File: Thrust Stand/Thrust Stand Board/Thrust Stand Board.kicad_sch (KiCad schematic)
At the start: 0 parts

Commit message: Components added for Thrust Stand Board
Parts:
- added J1: Conn_01x02_Socket, Package_QFP:TQFP-44_10x10mm_P0.8mm, symbol Connector:Conn_01x02_Socket
- added P1: USB_C_Plug_USB2.0, Package_DFN_QFN:UQFN-16_1.8x2.6mm_P0.4mm, symbol Connector:USB_C_Plug_USB2.0
- added U1: INA238, Package_SO:TSSOP-10_3x3mm_P0.5mm, symbol Sensor_Energy:INA238
- added U2: ACS758xCB-050B-PFF, Sensor_Current:Allegro_CB_PFF, symbol Sensor_Current:ACS758xCB-050B-PFF
- added U3: HX711, Package_SO:SOIC-16_3.9x9.9mm_P1.27mm, symbol Analog_ADC:HX711
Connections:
- new net: P1.A4 (VBUS), P1.A9 (VBUS), P1.B4 (VBUS), P1.B9 (VBUS)
- new net +BATT: J1.2 (Pin_2), U1.8 (Vbus)
- new net GND: J1.1 (Pin_1), P1.A1 (GND), P1.A12 (GND), P1.B1 (GND), P1.B12 (GND), P1.SH (SHIELD), U1.7 (GND)
- new net USBC_N: P1.A7 (D-)
- new net USBC_P: P1.A6 (D+)

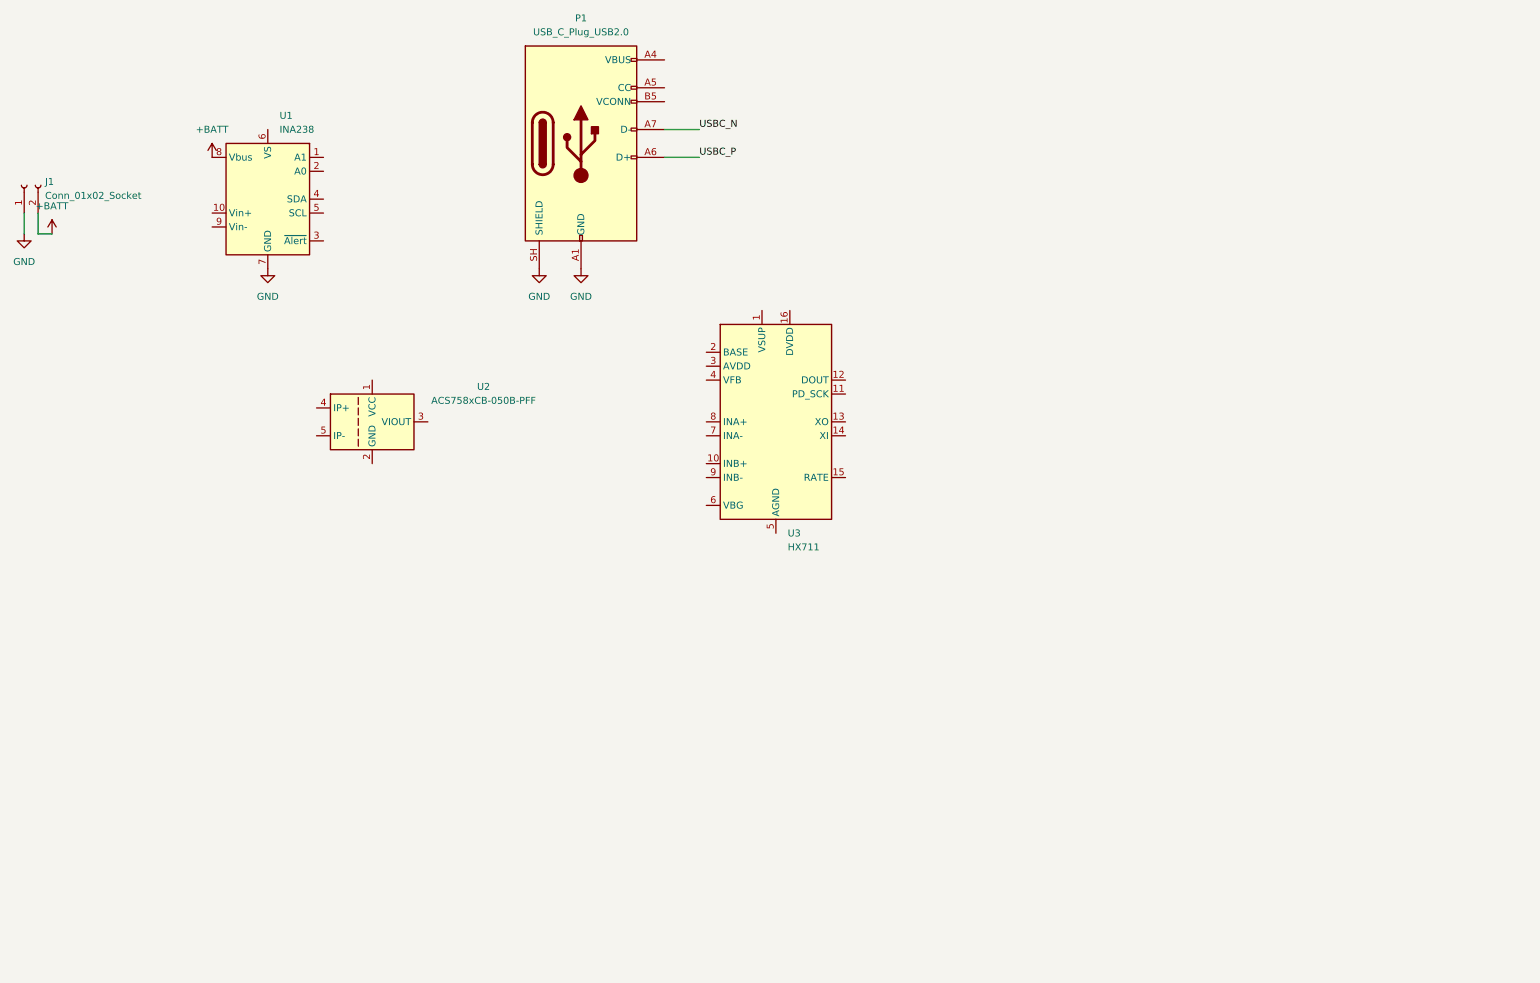
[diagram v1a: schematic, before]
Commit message: Schematic Updates
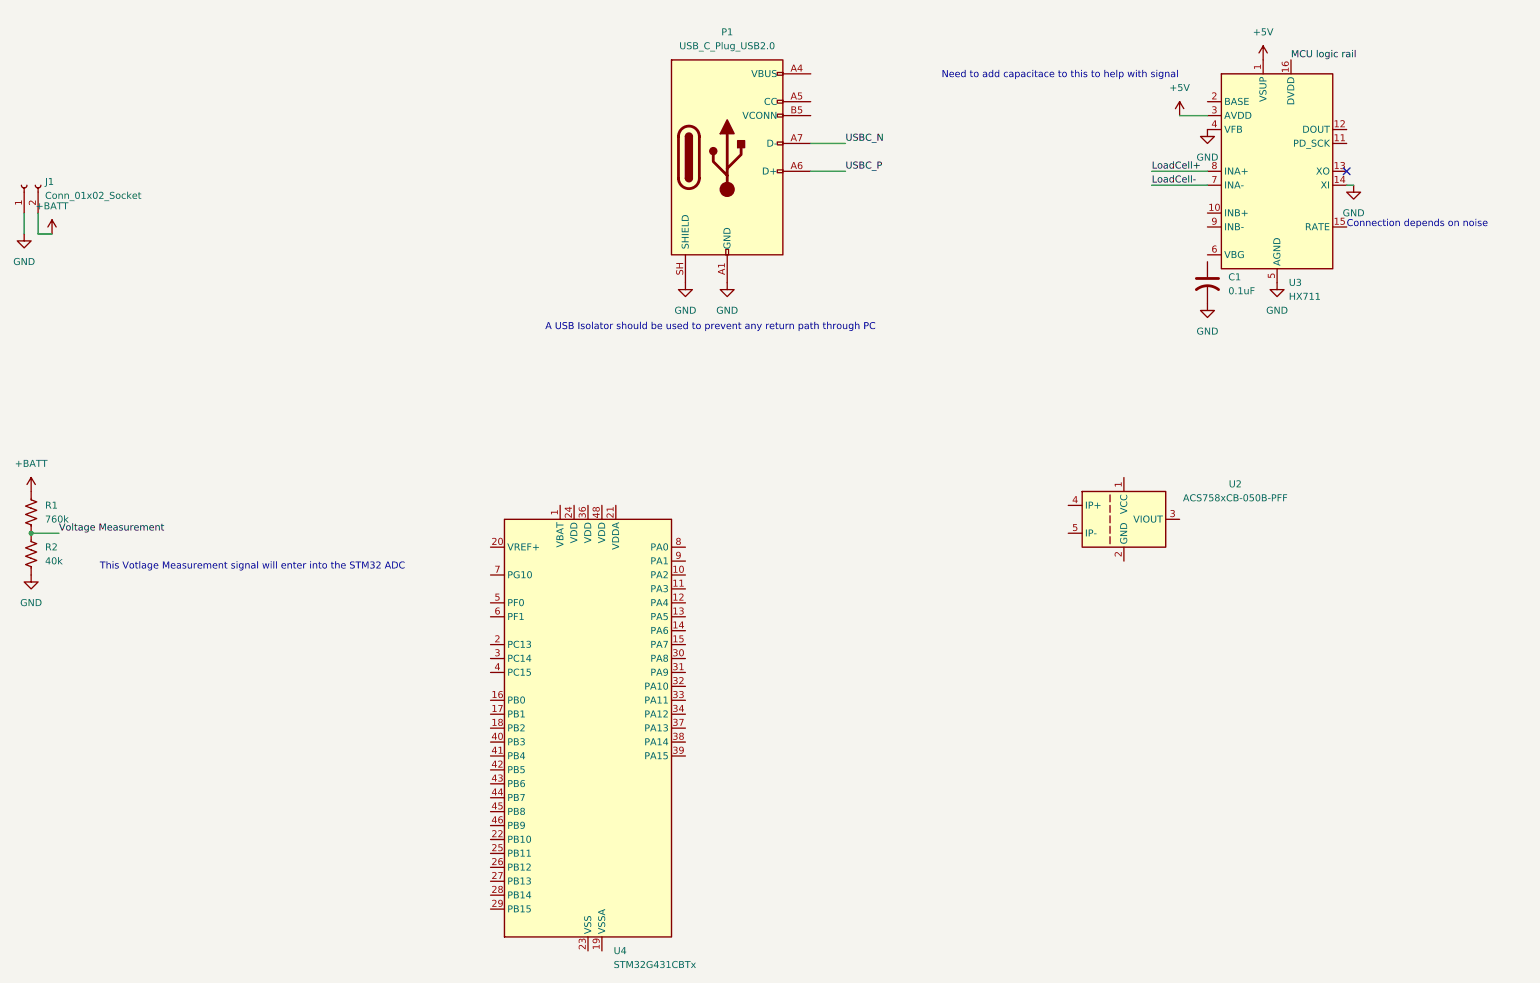
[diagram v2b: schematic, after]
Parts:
- removed U1: INA238, Package_SO:TSSOP-10_3x3mm_P0.5mm, symbol Sensor_Energy:INA238
- added C1: 0.1uF, Package_SO:SOIC-8_3.9x4.9mm_P1.27mm, symbol Device:C_US
- added R1: 760k, Package_QFP:LQFP-48_7x7mm_P0.5mm, symbol Device:R_US
- added R2: 40k, Package_QFP:LQFP-48_7x7mm_P0.5mm, symbol Device:R_US
- added U4: STM32G431CBTx, Package_QFP:LQFP-48_7x7mm_P0.5mm, symbol MCU_ST_STM32G4:STM32G431CBTx
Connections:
- net +BATT: now also R1.1
- net GND: now also U3.14 (XI), U3.4 (VFB), U3.5 (AGND), C1.2, R2.2
- net +5V: now reaches U3.1 (VSUP)
- net +5V: now also U3.3 (AVDD)
- net MCU logic rail: now reaches U3.16 (DVDD)
- net LoadCell-: now reaches U3.7 (INA-)
- net LoadCell+: now reaches U3.8 (INA+)
- new net: U4.23 (VSS), U4.35 (VSS), U4.47 (VSS)
- new net Voltage Measurement: R1.2, R2.1
- no-connect marks 0 -> 1
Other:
- note added: "A USB Isolator should be used to prevent any return path through PC"
- note added: "Connection depends on noise"
- note added: "Need to add capacitace to this to help with signal"
- note added: "This Votlage Measurement signal will enter into the STM32 ADC"
- moved on the sheet: P1, U2, U3
